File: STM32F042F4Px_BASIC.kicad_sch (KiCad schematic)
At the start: 5 parts, among them J11 TC2030-IDC, U1 STM32F042F4Px

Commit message: modified
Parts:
- renumbered C1 to C3, C2 to C4, C3 to C5, J11 to J12
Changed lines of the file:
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@@
   (symbol (lib_id "Device:C") (at 102.235 77.47 0) (unit 1)
     (in_bom yes) (on_board yes) (fields_autoplaced)
-    (property "Reference" "C1" (id 0) (at 105.156 76.5615 0)
+    (property "Reference" "C3" (id 0) (at 105.156 76.5615 0)
       (effects (font (size 1.27 1.27)) (justify left))
     )
@@
   (symbol (lib_id "Device:C") (at 125.73 77.47 0) (unit 1)
     (in_bom yes) (on_board yes) (fields_autoplaced)
-    (property "Reference" "C3" (id 0) (at 128.651 76.5615 0)
+    (property "Reference" "C5" (id 0) (at 128.651 76.5615 0)
       (effects (font (size 1.27 1.27)) (justify left))
     )
@@
   (symbol (lib_id "Device:C") (at 113.665 77.47 0) (unit 1)
     (in_bom yes) (on_board yes) (fields_autoplaced)
-    (property "Reference" "C2" (id 0) (at 116.586 76.5615 0)
+    (property "Reference" "C4" (id 0) (at 116.586 76.5615 0)
       (effects (font (size 1.27 1.27)) (justify left))
     )
@@
   (symbol (lib_id "william_connectors:TC2030-IDC") (at 73.025 100.33 0) (mirror y) (unit 1)
     (in_bom yes) (on_board yes) (fields_autoplaced)
-    (property "Reference" "J11" (id 0) (at 71.7549 85.0699 0))
+    (property "Reference" "J12" (id 0) (at 71.7549 85.0699 0))
     (property "Value" "TC2030-IDC" (id 1) (at 71.7549 87.845 0))
     (property "Footprint" "Connector:Tag-Connect_TC2030-IDC-FP_2x03_P1.27mm_Vertical" (id 2) (at 76.835 97.79 0)

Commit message: 24V updates
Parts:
- renumbered C3 to C11, C4 to C12, C5 to C13, J12 to J8, U1 to U3
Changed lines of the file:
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@@
   (symbol (lib_id "Device:C") (at 102.235 77.47 0) (unit 1)
     (in_bom yes) (on_board yes) (fields_autoplaced)
-    (property "Reference" "C3" (id 0) (at 105.156 76.5615 0)
+    (property "Reference" "C11" (id 0) (at 105.156 76.5615 0)
       (effects (font (size 1.27 1.27)) (justify left))
     )
@@
   (symbol (lib_id "MCU_ST_STM32F0:STM32F042F4Px") (at 168.91 97.79 0) (unit 1)
     (in_bom yes) (on_board yes)
-    (property "Reference" "U1" (id 0) (at 178.435 81.28 0)
+    (property "Reference" "U3" (id 0) (at 178.435 81.28 0)
       (effects (font (size 1.27 1.27)) (justify left))
     )
@@
   (symbol (lib_id "Device:C") (at 125.73 77.47 0) (unit 1)
     (in_bom yes) (on_board yes) (fields_autoplaced)
-    (property "Reference" "C5" (id 0) (at 128.651 76.5615 0)
+    (property "Reference" "C13" (id 0) (at 128.651 76.5615 0)
       (effects (font (size 1.27 1.27)) (justify left))
     )
@@
   (symbol (lib_id "Device:C") (at 113.665 77.47 0) (unit 1)
     (in_bom yes) (on_board yes) (fields_autoplaced)
-    (property "Reference" "C4" (id 0) (at 116.586 76.5615 0)
+    (property "Reference" "C12" (id 0) (at 116.586 76.5615 0)
       (effects (font (size 1.27 1.27)) (justify left))
     )
@@
   (symbol (lib_id "william_connectors:TC2030-IDC") (at 73.025 100.33 0) (mirror y) (unit 1)
     (in_bom yes) (on_board yes) (fields_autoplaced)
-    (property "Reference" "J12" (id 0) (at 71.7549 85.0699 0))
+    (property "Reference" "J8" (id 0) (at 71.7549 85.0699 0))
     (property "Value" "TC2030-IDC" (id 1) (at 71.7549 87.845 0))
     (property "Footprint" "Connector:Tag-Connect_TC2030-IDC-FP_2x03_P1.27mm_Vertical" (id 2) (at 76.835 97.79 0)

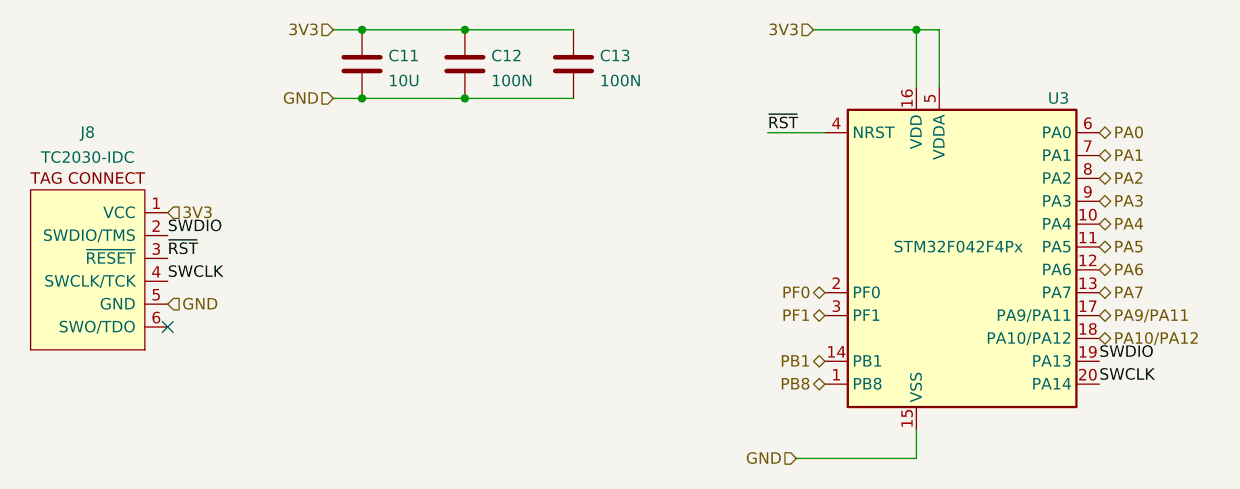
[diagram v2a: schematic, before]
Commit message: fix LT1161 symbol/sch
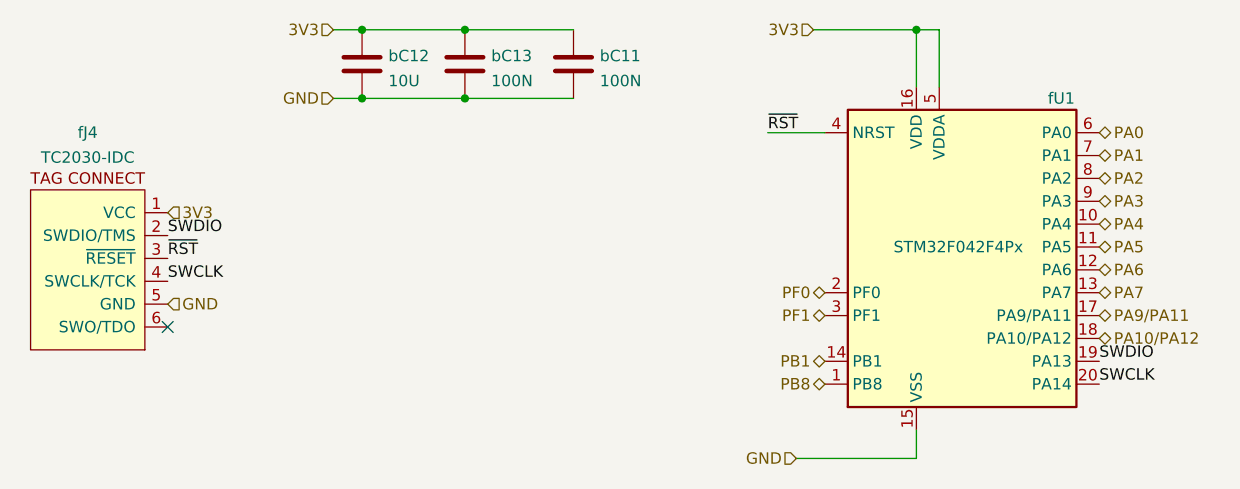
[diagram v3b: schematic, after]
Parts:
- renumbered C13 to bC11, C11 to bC12, C12 to bC13, J8 to fJ4, U3 to fU1
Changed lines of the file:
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@@
   (symbol (lib_id "Device:C") (at 102.235 77.47 0) (unit 1)
     (in_bom yes) (on_board yes) (fields_autoplaced)
-    (property "Reference" "C11" (id 0) (at 105.156 76.5615 0)
+    (property "Reference" "bC12" (id 0) (at 105.156 76.5615 0)
       (effects (font (size 1.27 1.27)) (justify left))
     )
@@
   (symbol (lib_id "MCU_ST_STM32F0:STM32F042F4Px") (at 168.91 97.79 0) (unit 1)
     (in_bom yes) (on_board yes)
-    (property "Reference" "U3" (id 0) (at 178.435 81.28 0)
+    (property "Reference" "fU1" (id 0) (at 178.435 81.28 0)
       (effects (font (size 1.27 1.27)) (justify left))
     )
@@
   (symbol (lib_id "Device:C") (at 125.73 77.47 0) (unit 1)
     (in_bom yes) (on_board yes) (fields_autoplaced)
-    (property "Reference" "C13" (id 0) (at 128.651 76.5615 0)
+    (property "Reference" "bC11" (id 0) (at 128.651 76.5615 0)
       (effects (font (size 1.27 1.27)) (justify left))
     )
@@
   (symbol (lib_id "Device:C") (at 113.665 77.47 0) (unit 1)
     (in_bom yes) (on_board yes) (fields_autoplaced)
-    (property "Reference" "C12" (id 0) (at 116.586 76.5615 0)
+    (property "Reference" "bC13" (id 0) (at 116.586 76.5615 0)
       (effects (font (size 1.27 1.27)) (justify left))
     )
@@
   (symbol (lib_id "william_connectors:TC2030-IDC") (at 73.025 100.33 0) (mirror y) (unit 1)
     (in_bom yes) (on_board yes) (fields_autoplaced)
-    (property "Reference" "J8" (id 0) (at 71.7549 85.0699 0))
+    (property "Reference" "fJ4" (id 0) (at 71.7549 85.0699 0))
     (property "Value" "TC2030-IDC" (id 1) (at 71.7549 87.845 0))
     (property "Footprint" "Connector:Tag-Connect_TC2030-IDC-FP_2x03_P1.27mm_Vertical" (id 2) (at 76.835 97.79 0)
